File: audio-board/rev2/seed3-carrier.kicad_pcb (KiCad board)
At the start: 4 copper layers, 90 x 56.5 mm, 59 parts, among them J1 NRJ4HF, J2 SJ3-35063AG, J3 DISPLAY_UART, J4 SJ3-35063AG, J5 LINE_OUT, J6 POWER_BOARD, Q1 AO3401A, Q2 2N7002, U1 TLV9061IDBVR, U2 TPA6132A2RTE

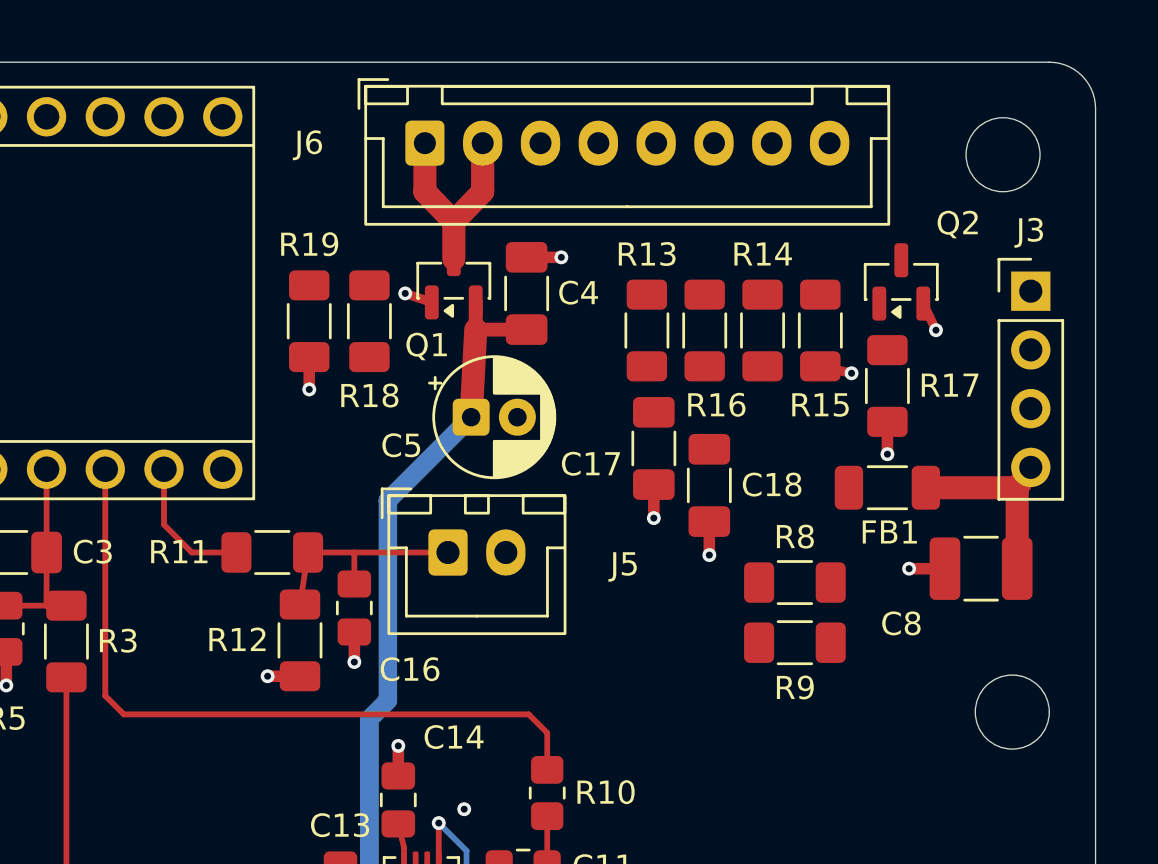
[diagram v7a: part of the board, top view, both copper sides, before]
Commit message: Use screw terminals for the power board, display and speaker connectors
J6 becomes a 4-way 3.5 mm screw terminal (5V, GND, BAT, MUTE) and J3 a
3-way (GND, TX, RX), side by side on the rear edge; J5 becomes a 2-way
(LINE+, LINE-) on the right edge. All three open toward the board edge and
have their terminal functions on the silkscreen. KF350-3.5 blocks from
LCSC; J6 is two 2-ways slid together.

The power button and PWR_HOLD move to the power board, so R14-R16 and C18
go and Daisy pins 26/27 become no-connects. The display is powered from the
power board, so FB1, C8 and DISPLAY_5V go. LINE- is LINE_REF, 1k to GND
through the new R21, to match R11's source impedance for the speaker amp's
differential input. R9 goes to 10k to match R8.

The parts under J6 and J3 are re-placed one column per terminal, and the
power entry, analog +5V branch start and speaker send are re-routed. ERC is
clean, the board check passes with no errors, and schematic parity holds.

Co-Authored-By: Claude Opus 5.5 <noreply@anthropic.com>
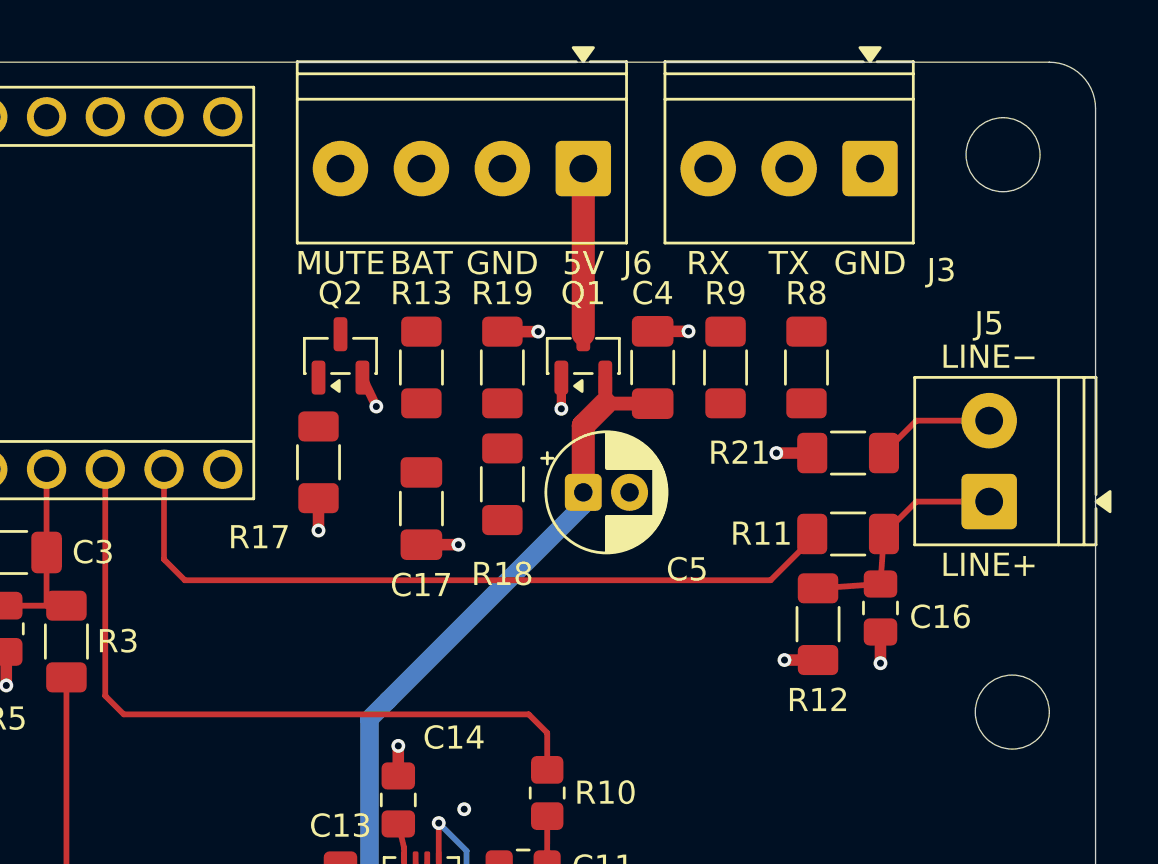
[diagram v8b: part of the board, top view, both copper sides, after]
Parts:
- removed C18: 100nF, Capacitor_SMD:C_1206_3216Metric_Pad1.33x1.80mm_HandSolder
- removed C8: 47uF 16V, Capacitor_SMD:C_1210_3225Metric_Pad1.33x2.70mm_HandSolder
- removed FB1: 600R@100MHz, Inductor_SMD:L_1206_3216Metric_Pad1.22x1.90mm_HandSolder
- removed R14, R16: 1k, Resistor_SMD:R_1206_3216Metric_Pad1.30x1.75mm_HandSolder
- removed R15: 100k, Resistor_SMD:R_1206_3216Metric_Pad1.30x1.75mm_HandSolder
- added R21: 1k, Resistor_SMD:R_1206_3216Metric_Pad1.30x1.75mm_HandSolder, F.Cu at (179.3, 66.9)
- J3: footprint Connector_PinHeader_2.54mm:PinHeader_1x04_P2.54mm_Vertical -> TerminalBlock_Phoenix:TerminalBlock_Phoenix_PT-1,5-3-3.5-H_1x03_P3.50mm_Horizontal
- J5: value LINE_OUT -> SPEAKER_SEND; footprint Connector_JST:JST_XH_B2B-XH-A_1x02_P2.50mm_Vertical -> TerminalBlock_Phoenix:TerminalBlock_Phoenix_PT-1,5-2-3.5-H_1x02_P3.50mm_Horizontal
- J6: footprint Connector_JST:JST_XH_B8B-XH-A_1x08_P2.50mm_Vertical -> TerminalBlock_Phoenix:TerminalBlock_Phoenix_PT-1,5-4-3.5-H_1x04_P3.50mm_Horizontal
- R9: value 1k -> 10k
- moved R11 24.9 mm to (179.3, 70.4)
- moved R17 24.8 mm to (156.4, 67.3)
- moved Q2 24.5 mm to (157.3, 62.7)
- moved J5 23.5 mm to (185.4, 69.0), turned to 90 degrees
- moved C16 22.8 mm to (180.7, 73.6)
- moved R12 22.4 mm to (178.0, 74.3)
- moved R9 12.3 mm to (174.0, 63.2), turned to -90 degrees
- moved C17 10.4 mm to (160.8, 69.3)
- moved R13 9.88 mm to (160.8, 63.2)
- moved R8 9.31 mm to (177.5, 63.2), turned to 90 degrees
- moved R18 9.10 mm to (164.3, 68.2)
- moved J3 8.74 mm to (180.2, 54.6), turned to 180 degrees
- moved R19 8.59 mm to (164.3, 63.2), turned to 90 degrees
- moved J6 6.94 mm to (167.8, 54.6), turned to 180 degrees
- moved Q1 6.47 mm to (167.8, 62.7)
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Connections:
- A1 pad 26: /PWR_BTN -> unconnected-(A1-ADC_4-Pad26)
- A1 pad 27: /PWR_HOLD -> unconnected-(A1-ADC_5-Pad27)
- J5 pad 2: GND -> /LINE_REF
- J6 pad 2: /5V_IN -> GND
- J6 pad 3: GND -> /BATT_SENSE_CONN
- J6 pad 4: GND -> /SPK_MUTE
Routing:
- net /AUDIO_OUT_2: track 6.03 -> 33.2 mm
- net /DISPLAY_5V: track 8.51 -> 0.00 mm
- net /LINE_REF: track 0.00 -> 5.13 mm
- net /5V_IN: track 9.42 -> 7.16 mm
- net GND: track 58.6 -> 56.5 mm, vias 35 -> 33
- net +5V: track 92.1 -> 91.0 mm
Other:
- board text added: "5V"
- board text added: "BAT"
- board text added: "GND"
- board text added: "LINE+"
- board text added: "LINE−"
- board text added: "MUTE"
- board text added: "RX"
- board text added: "TX"
